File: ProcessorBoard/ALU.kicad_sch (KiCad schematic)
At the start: 2 parts, among them U47 IDT7381

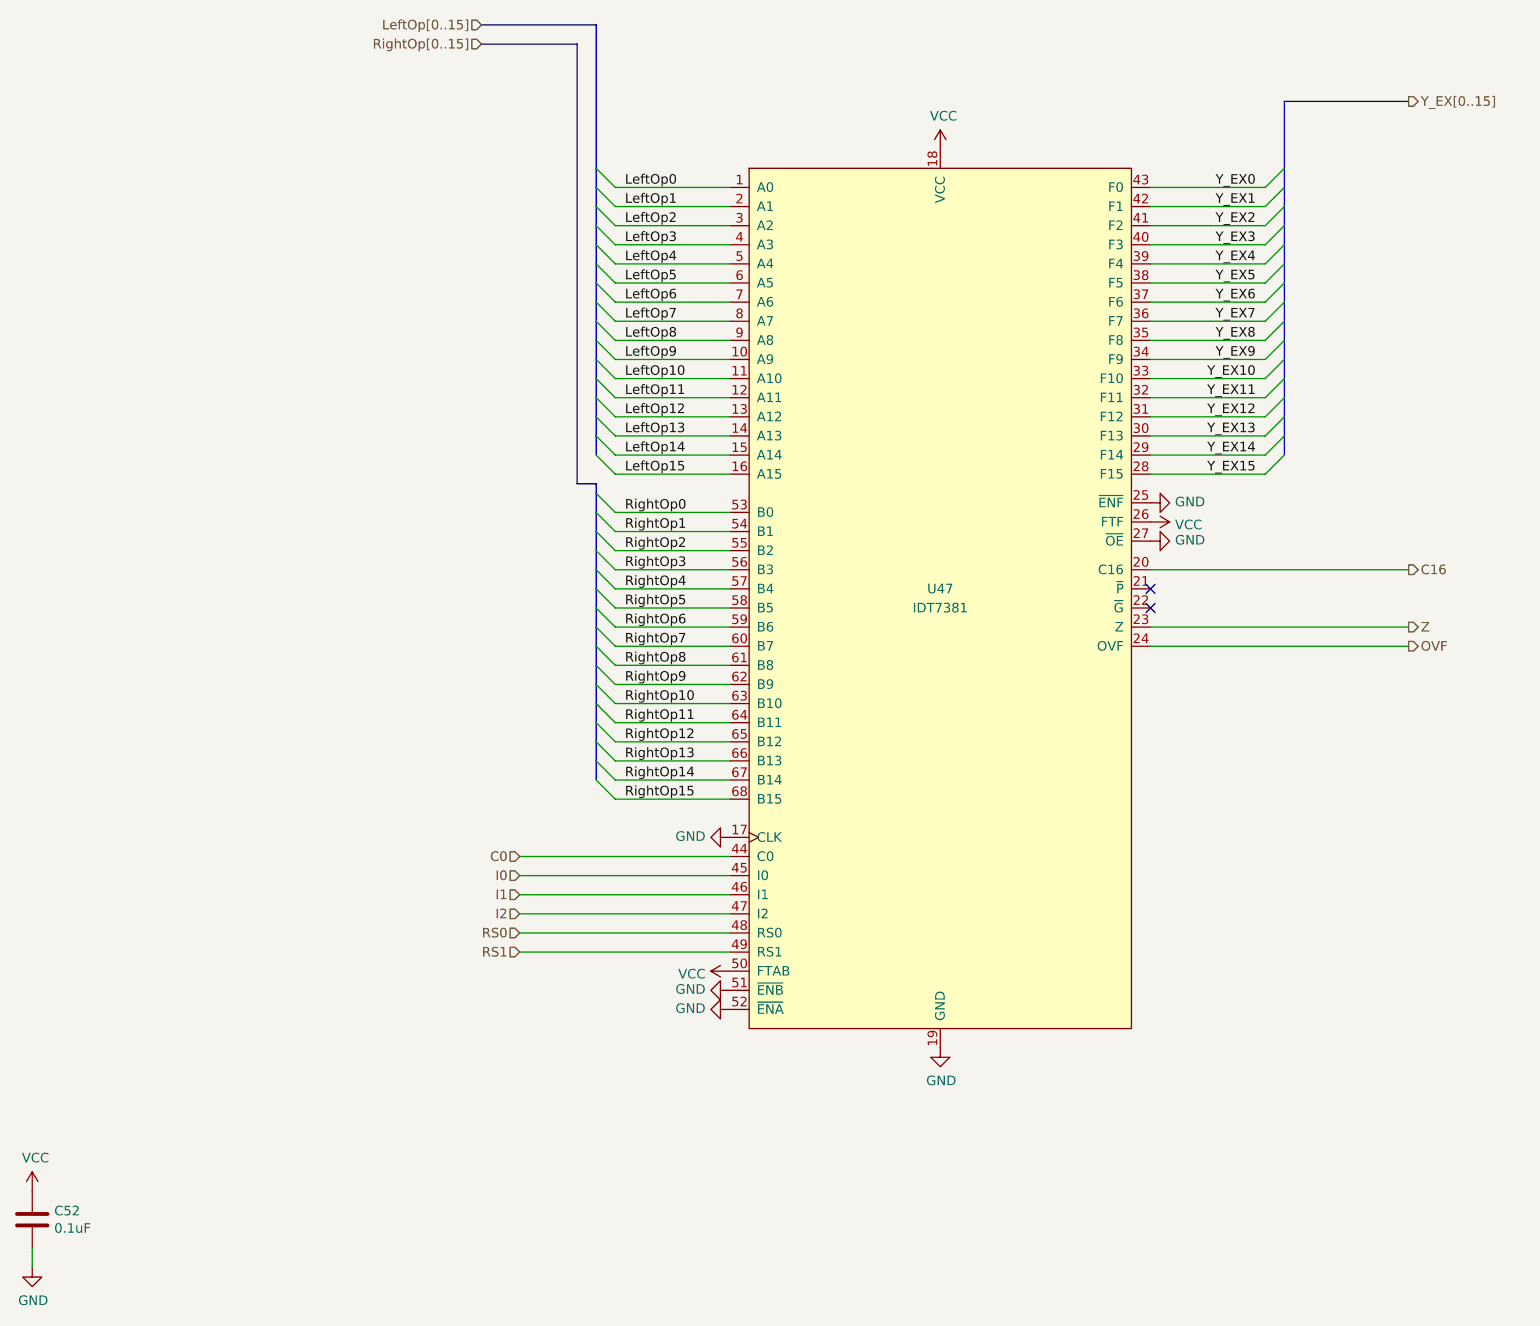
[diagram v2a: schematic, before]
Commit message: ProcessorBoard: update to include M/S bug fix in register file
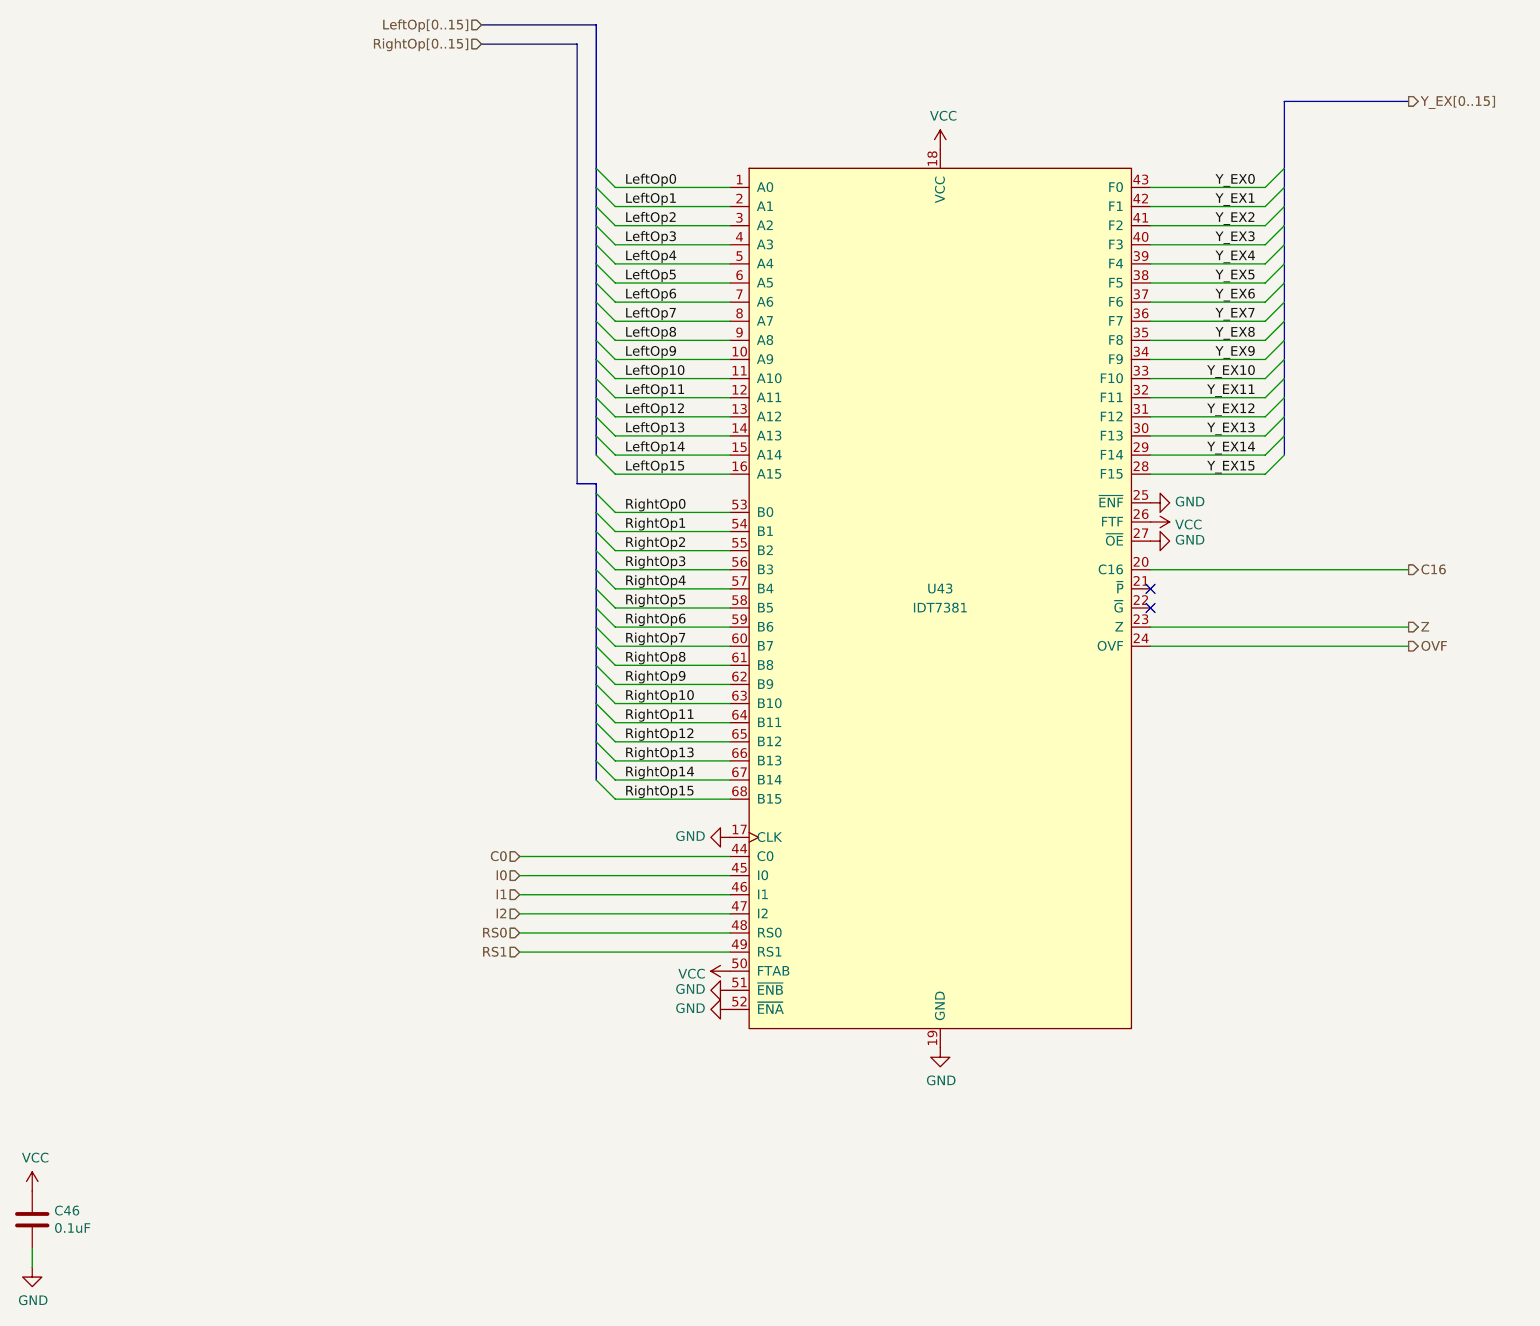
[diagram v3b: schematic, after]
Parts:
- renumbered C52 to C46, U47 to U43
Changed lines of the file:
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@@
   (symbol (lib_id "Device:C") (at 21.59 185.42 0) (unit 1)
     (in_bom yes) (on_board yes) (dnp no)
-    (property "Reference" "C52" (at 24.511 184.2516 0)
+    (property "Reference" "C46" (at 24.511 184.2516 0)
       (effects (font (size 1.27 1.27)) (justify left))
     )
@@
       (project "ProcessorBoard"
         (path "/83c5181e-f5ee-453c-ae5c-d7256ba8837d/00000000-0000-0000-0000-000060a71bbf/00000000-0000-0000-0000-00005fc6fe4b"
-          (reference "C52") (unit 1)
+          (reference "C46") (unit 1)
         )
       )
@@
   (symbol (lib_id "power:VCC") (at 21.59 181.61 0) (unit 1)
     (in_bom yes) (on_board yes) (dnp no)
-    (property "Reference" "#PWR0311" (at 21.59 185.42 0)
+    (property "Reference" "#PWR0293" (at 21.59 185.42 0)
       (effects (font (size 1.27 1.27)) hide)
     )
@@
       (project "ProcessorBoard"
         (path "/83c5181e-f5ee-453c-ae5c-d7256ba8837d/00000000-0000-0000-0000-000060a71bbf/00000000-0000-0000-0000-00005fc6fe4b"
-          (reference "#PWR0311") (unit 1)
+          (reference "#PWR0293") (unit 1)
         )
       )
@@
   (symbol (lib_id "power:GND") (at 21.59 191.77 0) (unit 1)
     (in_bom yes) (on_board yes) (dnp no)
-    (property "Reference" "#PWR0312" (at 21.59 198.12 0)
+    (property "Reference" "#PWR0294" (at 21.59 198.12 0)
       (effects (font (size 1.27 1.27)) hide)
     )
@@
       (project "ProcessorBoard"
         (path "/83c5181e-f5ee-453c-ae5c-d7256ba8837d/00000000-0000-0000-0000-000060a71bbf/00000000-0000-0000-0000-00005fc6fe4b"
-          (reference "#PWR0312") (unit 1)
+          (reference "#PWR0294") (unit 1)
         )
       )
@@
   (symbol (lib_id "EXModule-rescue:IDT7381-CPU") (at 142.24 102.87 0) (unit 1)
     (in_bom yes) (on_board yes) (dnp no)
-    (property "Reference" "U47" (at 142.24 101.6 0)
+    (property "Reference" "U43" (at 142.24 101.6 0)
       (effects (font (size 1.27 1.27)))
     )
@@
       (project "ProcessorBoard"
         (path "/83c5181e-f5ee-453c-ae5c-d7256ba8837d/00000000-0000-0000-0000-000060a71bbf/00000000-0000-0000-0000-00005fc6fe4b"
-          (reference "U47") (unit 1)
+          (reference "U43") (unit 1)
         )
       )
@@
   (symbol (lib_id "power:VCC") (at 142.24 43.18 0) (unit 1)
     (in_bom yes) (on_board yes) (dnp no)
-    (property "Reference" "#PWR0317" (at 142.24 46.99 0)
+    (property "Reference" "#PWR0299" (at 142.24 46.99 0)
       (effects (font (size 1.27 1.27)) hide)
     )
@@
       (project "ProcessorBoard"
         (path "/83c5181e-f5ee-453c-ae5c-d7256ba8837d/00000000-0000-0000-0000-000060a71bbf/00000000-0000-0000-0000-00005fc6fe4b"
-          (reference "#PWR0317") (unit 1)
+          (reference "#PWR0299") (unit 1)
         )
       )
@@
   (symbol (lib_id "power:GND") (at 142.24 162.56 0) (unit 1)
     (in_bom yes) (on_board yes) (dnp no)
-    (property "Reference" "#PWR0318" (at 142.24 168.91 0)
+    (property "Reference" "#PWR0300" (at 142.24 168.91 0)
       (effects (font (size 1.27 1.27)) hide)
     )
@@
       (project "ProcessorBoard"
         (path "/83c5181e-f5ee-453c-ae5c-d7256ba8837d/00000000-0000-0000-0000-000060a71bbf/00000000-0000-0000-0000-00005fc6fe4b"
-          (reference "#PWR0318") (unit 1)
+          (reference "#PWR0300") (unit 1)
         )
       )
@@
   (symbol (lib_id "power:GND") (at 170.18 90.17 90) (unit 1)
     (in_bom yes) (on_board yes) (dnp no)
-    (property "Reference" "#PWR0319" (at 176.53 90.17 0)
+    (property "Reference" "#PWR0301" (at 176.53 90.17 0)
       (effects (font (size 1.27 1.27)) hide)
     )
@@
       (project "ProcessorBoard"
         (path "/83c5181e-f5ee-453c-ae5c-d7256ba8837d/00000000-0000-0000-0000-000060a71bbf/00000000-0000-0000-0000-00005fc6fe4b"
-          (reference "#PWR0319") (unit 1)
+          (reference "#PWR0301") (unit 1)
         )
       )
@@
   (symbol (lib_id "power:GND") (at 114.3 154.94 270) (mirror x) (unit 1)
     (in_bom yes) (on_board yes) (dnp no)
-    (property "Reference" "#PWR0315" (at 107.95 154.94 0)
+    (property "Reference" "#PWR0297" (at 107.95 154.94 0)
       (effects (font (size 1.27 1.27)) hide)
     )
@@
       (project "ProcessorBoard"
         (path "/83c5181e-f5ee-453c-ae5c-d7256ba8837d/00000000-0000-0000-0000-000060a71bbf/00000000-0000-0000-0000-00005fc6fe4b"
-          (reference "#PWR0315") (unit 1)
+          (reference "#PWR0297") (unit 1)
         )
       )
@@
   (symbol (lib_id "power:GND") (at 114.3 157.48 270) (mirror x) (unit 1)
     (in_bom yes) (on_board yes) (dnp no)
-    (property "Reference" "#PWR0316" (at 107.95 157.48 0)
+    (property "Reference" "#PWR0298" (at 107.95 157.48 0)
       (effects (font (size 1.27 1.27)) hide)
     )
@@
       (project "ProcessorBoard"
         (path "/83c5181e-f5ee-453c-ae5c-d7256ba8837d/00000000-0000-0000-0000-000060a71bbf/00000000-0000-0000-0000-00005fc6fe4b"
-          (reference "#PWR0316") (unit 1)
+          (reference "#PWR0298") (unit 1)
         )
       )
@@
   (symbol (lib_id "power:VCC") (at 170.18 92.71 270) (unit 1)
     (in_bom yes) (on_board yes) (dnp no)
-    (property "Reference" "#PWR0320" (at 166.37 92.71 0)
+    (property "Reference" "#PWR0302" (at 166.37 92.71 0)
       (effects (font (size 1.27 1.27)) hide)
     )
@@
       (project "ProcessorBoard"
         (path "/83c5181e-f5ee-453c-ae5c-d7256ba8837d/00000000-0000-0000-0000-000060a71bbf/00000000-0000-0000-0000-00005fc6fe4b"
-          (reference "#PWR0320") (unit 1)
+          (reference "#PWR0302") (unit 1)
         )
       )
@@
   (symbol (lib_id "power:GND") (at 114.3 134.62 270) (mirror x) (unit 1)
     (in_bom yes) (on_board yes) (dnp no)
-    (property "Reference" "#PWR0313" (at 107.95 134.62 0)
+    (property "Reference" "#PWR0295" (at 107.95 134.62 0)
       (effects (font (size 1.27 1.27)) hide)
     )
@@
       (project "ProcessorBoard"
         (path "/83c5181e-f5ee-453c-ae5c-d7256ba8837d/00000000-0000-0000-0000-000060a71bbf/00000000-0000-0000-0000-00005fc6fe4b"
-          (reference "#PWR0313") (unit 1)
+          (reference "#PWR0295") (unit 1)
         )
       )
@@
   (symbol (lib_id "power:VCC") (at 114.3 152.4 90) (mirror x) (unit 1)
     (in_bom yes) (on_board yes) (dnp no)
-    (property "Reference" "#PWR0314" (at 118.11 152.4 0)
+    (property "Reference" "#PWR0296" (at 118.11 152.4 0)
       (effects (font (size 1.27 1.27)) hide)
     )
@@
       (project "ProcessorBoard"
         (path "/83c5181e-f5ee-453c-ae5c-d7256ba8837d/00000000-0000-0000-0000-000060a71bbf/00000000-0000-0000-0000-00005fc6fe4b"
-          (reference "#PWR0314") (unit 1)
+          (reference "#PWR0296") (unit 1)
         )
       )
@@
   (symbol (lib_id "power:GND") (at 170.18 95.25 90) (unit 1)
     (in_bom yes) (on_board yes) (dnp no)
-    (property "Reference" "#PWR0321" (at 176.53 95.25 0)
+    (property "Reference" "#PWR0303" (at 176.53 95.25 0)
       (effects (font (size 1.27 1.27)) hide)
     )
@@
       (project "ProcessorBoard"
         (path "/83c5181e-f5ee-453c-ae5c-d7256ba8837d/00000000-0000-0000-0000-000060a71bbf/00000000-0000-0000-0000-00005fc6fe4b"
-          (reference "#PWR0321") (unit 1)
-        )
-      )
+          (reference "#PWR0303") (unit 1)
+        )
+      )
